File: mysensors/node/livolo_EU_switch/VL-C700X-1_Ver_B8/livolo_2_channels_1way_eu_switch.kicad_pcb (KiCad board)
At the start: 2 copper layers, 43.4 x 43.6 mm, 52 parts, among them CON1 AVR-ISP-6, IC1 ATMEGA328P-AU, P1 Sense Pad 1, P2 Sense Pad 2, P3 ANTENNA, P4 Power Board, U1 MIC5205-3.3, U2 MCP16301, U3 TTP223, U4 TTP223, U5 RFM69CW, U6 AT25DF512C-SSHN-B, U7 ATSHA204A

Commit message: [mysensors][livolo_EU_switch][VL-C700X-1_Ver_C2][1_channel] initial draft
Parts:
- REF**: footprint myfootprints:Livolo_EU_SW_2Ways_Frame -> myfootprints:Livolo_EU_SW_2_Channel_1Way_Frame_VL-C700X-1_Ver_B8

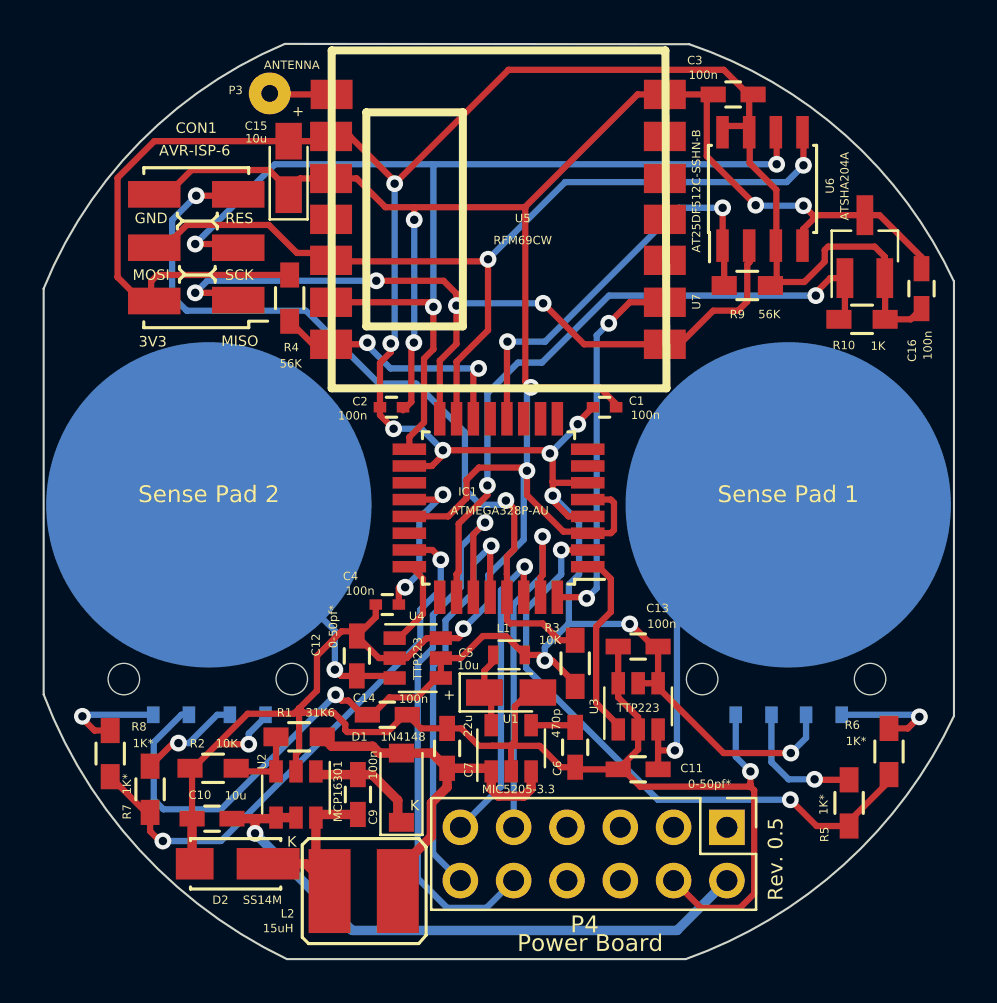
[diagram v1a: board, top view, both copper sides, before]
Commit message: [mysensors][livolo_EU_switch][VL-C700X-1_Ver_B8] added ground fill plane
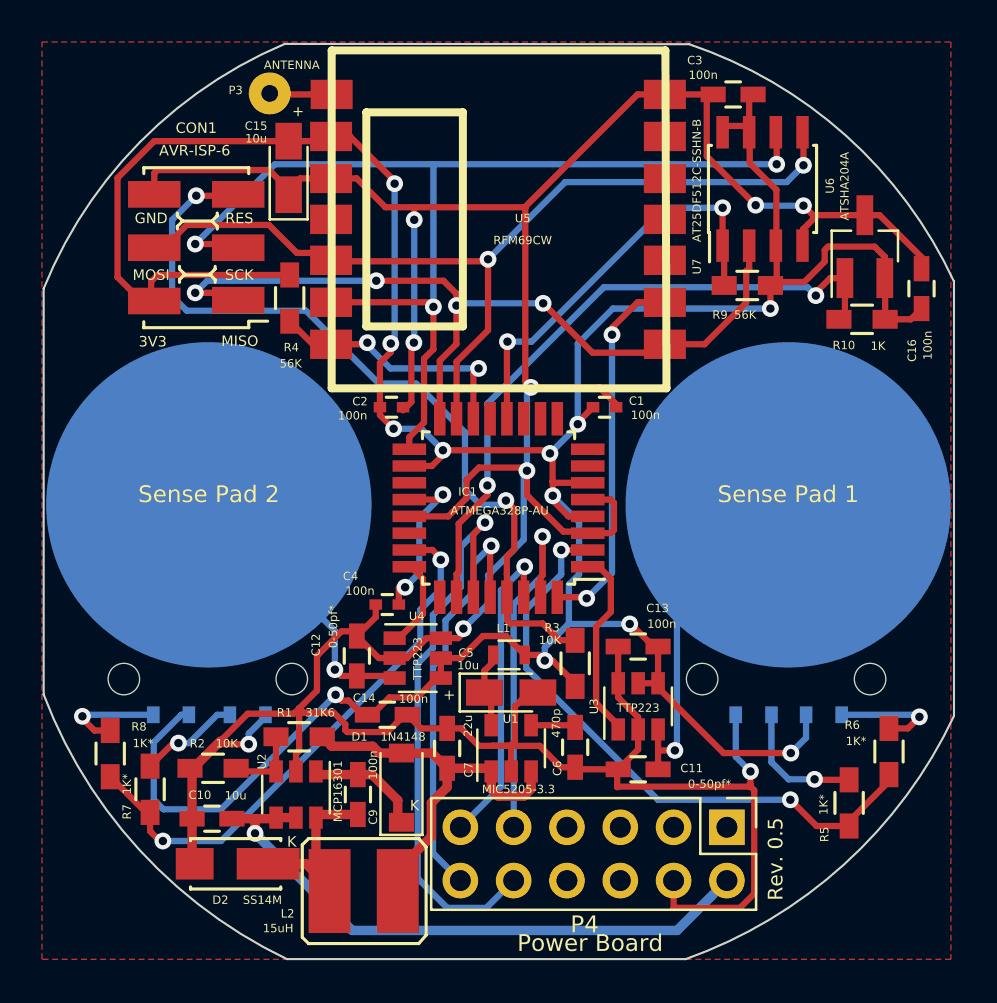
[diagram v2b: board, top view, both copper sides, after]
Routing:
- net +3V3: track 162.1 -> 157.3 mm, vias 11 -> 12
- net GND: track 182.0 -> 183.9 mm
- net /MISO: track 39.8 -> 40.6 mm
- added copper zone on F.Cu, net GND
